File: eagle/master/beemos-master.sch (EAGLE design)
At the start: 47 parts, among them CON1 BAT, CON2 JACK_DC_BARREL, CON3 SPI, IC1 32U4, IC2 MCP73831T, IC3 MCP1703CB, IC4 DMP1045U, J1 RJ123.3, J10 RJ12STRAIGHT-I2C, J2 RJ123.3, J3 RJ123.3, J4 RJ123.3, J5 RJ123.3, J6 RJ123.3, J8 RJ123.3, J9 RJ12STRAIGHT-I2C, X1 8MHz, X2 MINI-USB

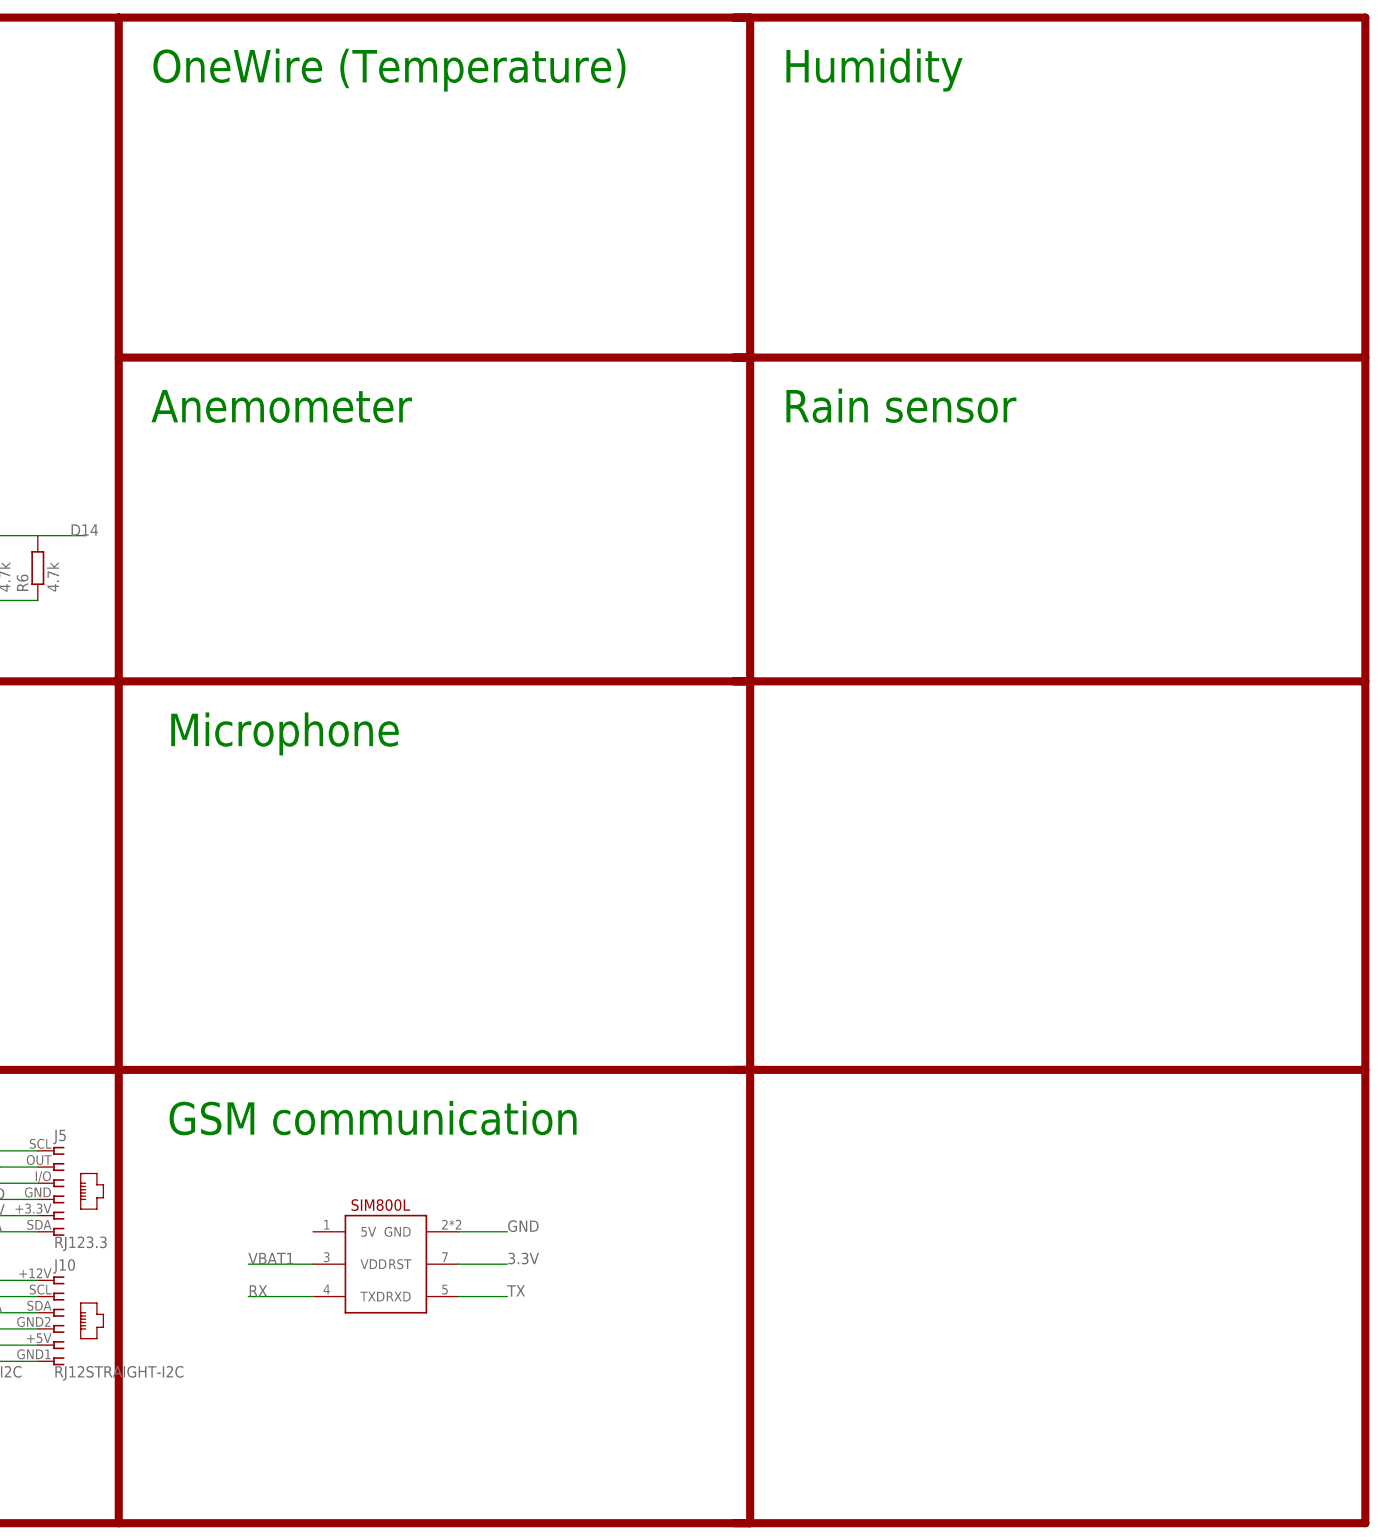
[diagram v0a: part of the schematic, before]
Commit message: Added LoRa and OneWire to schematics
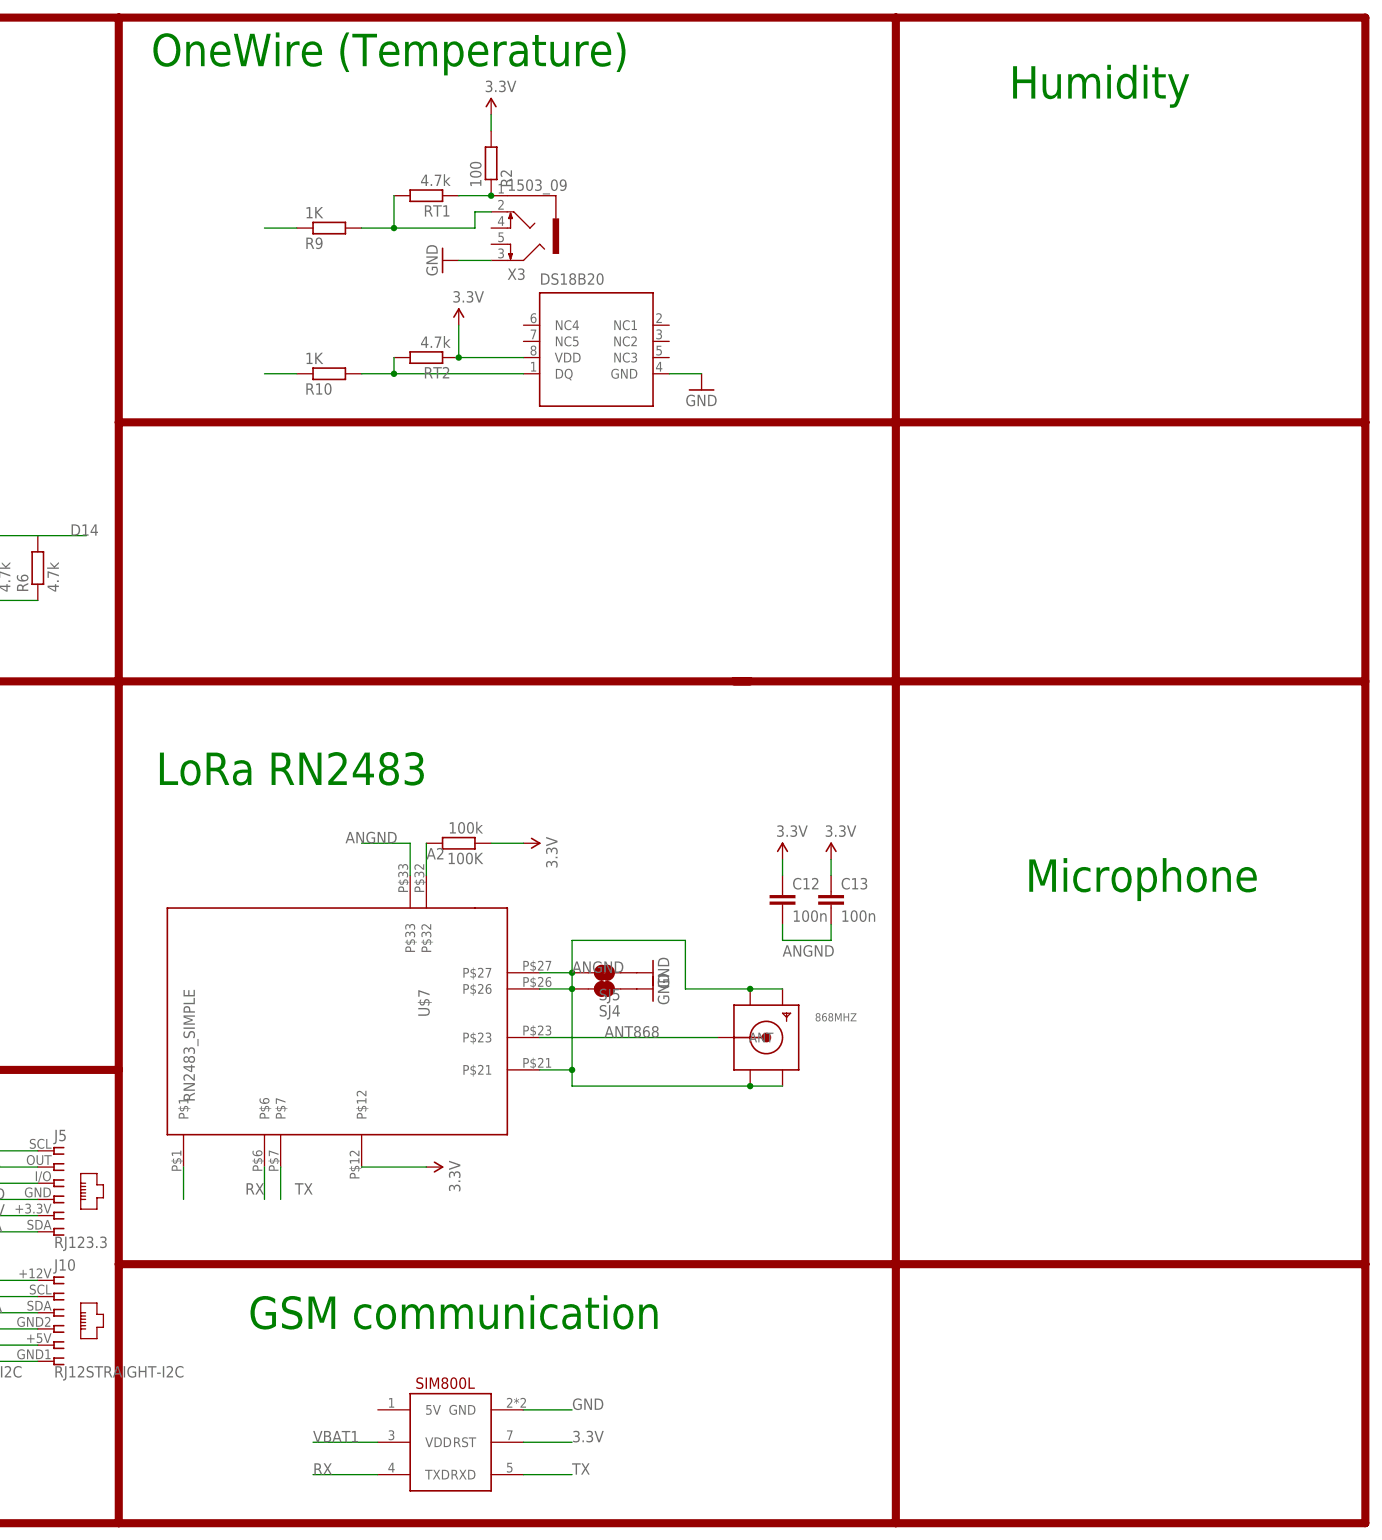
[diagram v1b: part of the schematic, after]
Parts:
- added 100K: 100k, rcl:R-EU_R0805
- added 868MHZ: (no value), sma_end_launch:SMACONNECTOR_EDGE_UFL
- added C12, C13: 100n, rcl:C-EUC0805
- added R10, R9: 1K, rcl:R-EU_R0805
- added R2: 100, rcl:R-EU_R0805
- added RT1, RT2: 4.7k, resistor:R-EU_R0805
- added SJ4, SJ5: JUMPER-PAD-2-NC_BY_TRACE, SparkFun-Passives:JUMPER-PAD-2-NC_BY_TRACE
- added U$7: RN2483_SIMPLE, Octanis1_bioreactorPort:RN2483_SIMPLE
- added U$8: DS18B20, lpatiny:DS18B20SMALL
- added X3: 1503_09, con-lumberg:1503_09
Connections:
- new net A7: R9.1
- new net ANGND: 868MHZ.GND1, 868MHZ.GND2, 868MHZ.GND3, 868MHZ.GND4, C12.2, C13.2, SJ4.2, SJ5.2, U$7.P$1, U$7.P$21, U$7.P$26, U$7.P$27, U$7.P$33
- new net ANT868: 868MHZ.ANT, U$7.P$23
- new net D12*: R10.1
- new net N$14: R2.1, RT1.1, X3.1
- new net N$21: R9.2, RT1.2, X3.2
- new net N$9: R10.2, RT2.2, U$8.DQ
- net 3.3V: now also 100K.1, C12.1, C13.1, R2.2, RT2.1, U$7.P$12, U$8.VDD
- net A2: now also 100K.2, U$7.P$32
- net GND: now also SJ4.1, SJ5.1, U$8.GND, X3.3
- net RX: now also U$7.P$6
- net TX: now also U$7.P$7
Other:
- note added: "LoRa RN2483"
- note removed: "Anemometer"
- note removed: "Rain sensor"

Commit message: added bee counter PCB soldering doc v1.0
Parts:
- added IC5: MS5637WIDE, MS5637:MS5637WIDE
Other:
- note added: "Barometric pressure"
- note removed: "Microphone"
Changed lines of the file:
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@@
 <part name="U$8" library="lpatiny" deviceset="DS18B20" device="SMALL" value="DS18B20"/>
 <part name="R2" library="rcl" deviceset="R-EU_" device="R0805" value="100"/>
+<part name="IC5" library="MS5637" deviceset="MS5637" device="WIDE"/>
 </parts>
 <sheets>
@@
 <wire x1="55.88" y1="198.12" x2="55.88" y2="129.54" width="1.524" layer="94"/>
 <wire x1="55.88" y1="198.12" x2="-15.24" y2="198.12" width="1.524" layer="94"/>
-<text x="347.98" y="96.52" size="5.08" layer="91">Microphone</text>
+<text x="330.2" y="119.38" size="5.08" layer="91">Barometric pressure</text>
 <text x="0" y="187.96" size="5.08" layer="91">MEMORY</text>
 <wire x1="327.66" y1="-2.54" x2="327.66" y2="233.68" width="1.27" layer="94"/>
@@
 <instance part="U$8" gate="G$1" x="281.94" y="180.34"/>
 <instance part="R2" gate="G$1" x="264.16" y="210.82" rot="MR90"/>
+<instance part="IC5" gate="G$1" x="365.76" y="83.82"/>
 </instances>
 <busses>
